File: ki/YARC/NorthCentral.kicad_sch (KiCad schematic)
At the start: 0 parts

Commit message: Continue annotating and labeling ICs
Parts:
- added U102, U103: 74HC245, symbol 74xx:74HC245
- added U88: 74HC00, symbol 74xx:74HC00
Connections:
- new net: U102.19 (CE), U103.19 (CE), U88.11
- new net GND: U102.10 (GND), U103.10 (GND)
- new net S1BUS0: U103.2 (A0)
- new net S1BUS15: U102.9 (A7)
- new net S1BUS7: U103.9 (A7)
- new net S1BUS8: U102.2 (A0)
- new net SYSADDR0: U103.18 (B0)
- new net SYSADDR15: U102.11 (B7)
- new net SYSADDR7: U103.11 (B7)
- new net SYSADDR8: U102.18 (B0)
- new net VCC: U102.1 (A->B), U102.20 (VCC), U103.1 (A->B), U103.20 (VCC)
- new net YARC/~{NANO}: U88.12, U88.13
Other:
- note added: "THIS SHEET IS ACTUALLY "EAST" CENTRAL"

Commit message: Minor changes while wiring Port1 address transceiver
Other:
- note added: "<== THIS IS WRONG - the signal comes from a '157. TODO."
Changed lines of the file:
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@@
+    (effects (font (size 1.27 1.27)) (justify left bottom))
+  )
+  (text "<== THIS IS WRONG - the signal comes from a '157. TODO."
+    (at 38.1 124.46 0)
     (effects (font (size 1.27 1.27)) (justify left bottom))
   )

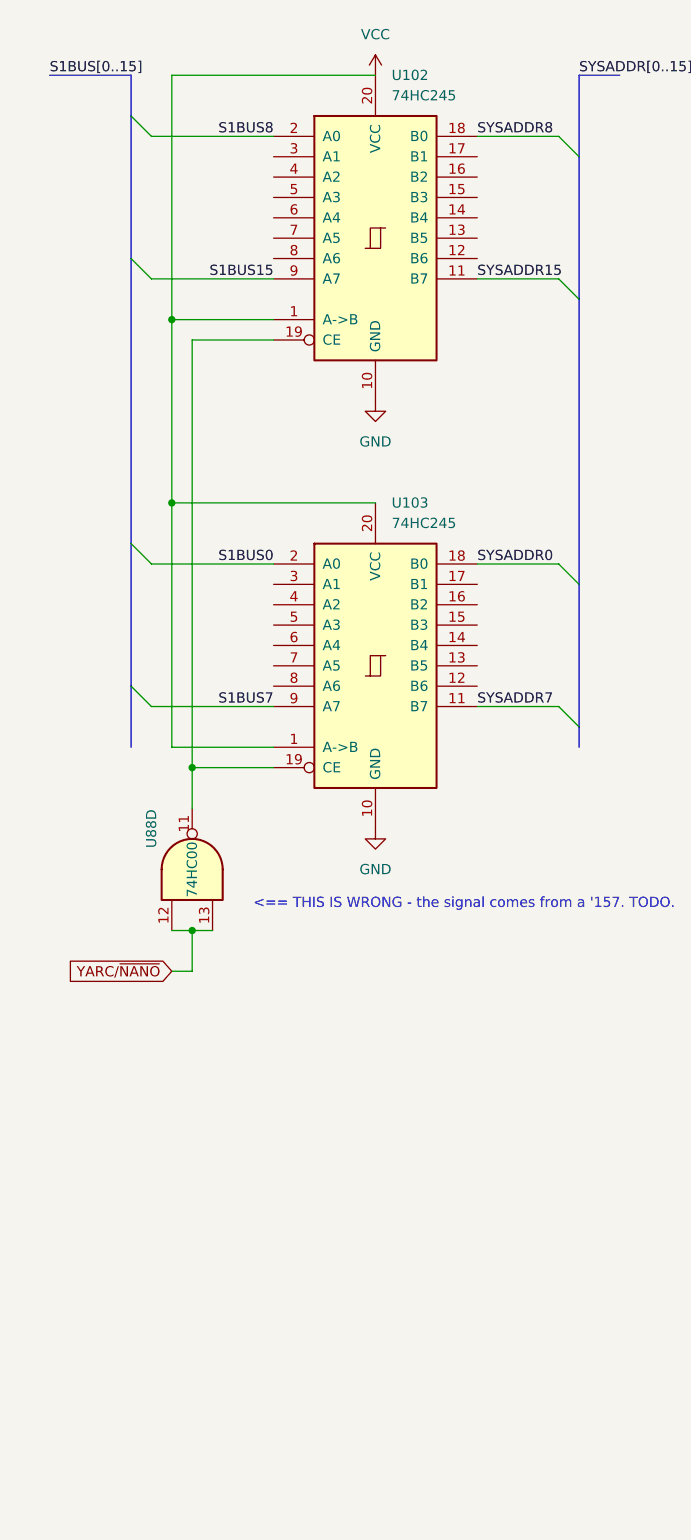
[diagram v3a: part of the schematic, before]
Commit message: Further development of ALU controls
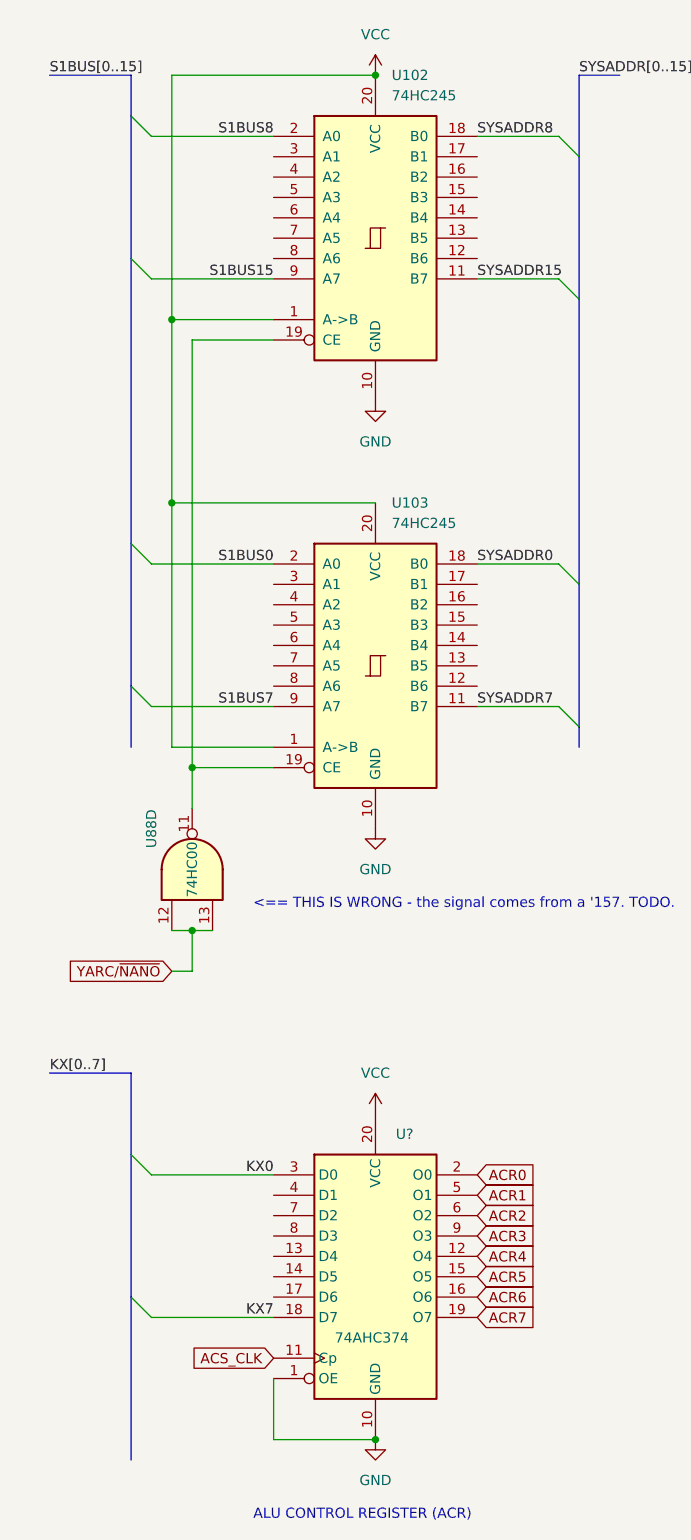
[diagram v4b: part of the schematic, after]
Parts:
- added U?: 74AHC374, symbol 74xx:74AHC374
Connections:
- net GND: now also U?.1 (OE), U?.10 (GND)
- net VCC: now also U?.20 (VCC)
- new net ACR0: U?.2 (O0)
- new net ACR1: U?.5 (O1)
- new net ACR2: U?.6 (O2)
- new net ACR3: U?.9 (O3)
- new net ACR4: U?.12 (O4)
- new net ACR5: U?.15 (O5)
- new net ACR6: U?.16 (O6)
- new net ACR7: U?.19 (O7)
- new net ACS_CLK: U?.11 (Cp)
- new net KX0: U?.3 (D0)
- new net KX7: U?.18 (D7)
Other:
- note added: "ALU CONTROL REGISTER (ACR)"

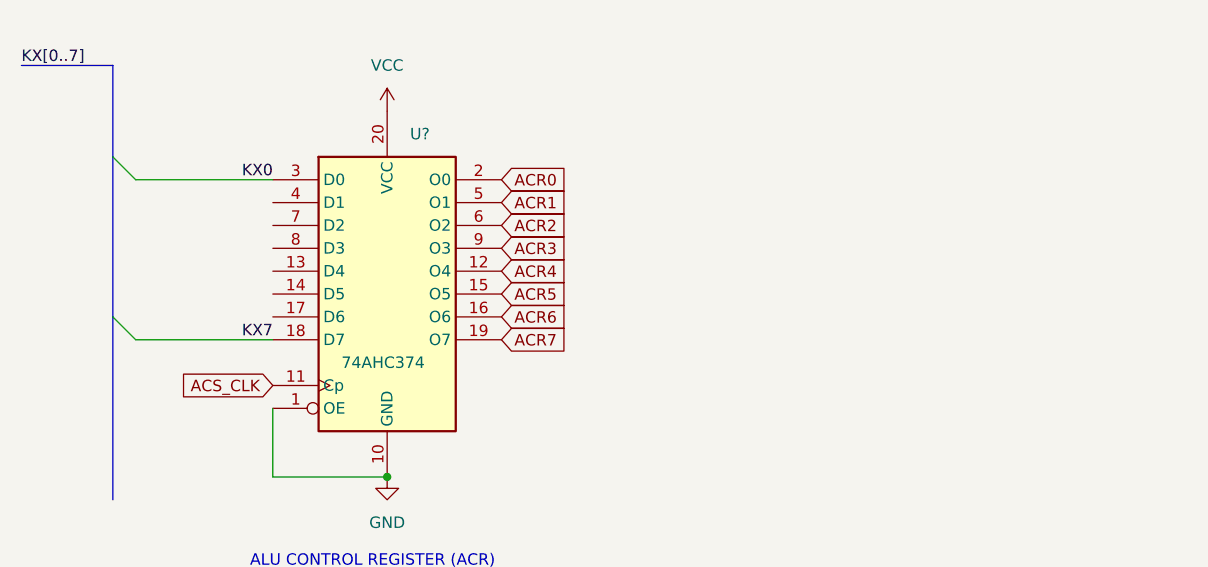
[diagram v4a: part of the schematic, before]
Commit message: ALU schematic checking complete. Ready to start layout.
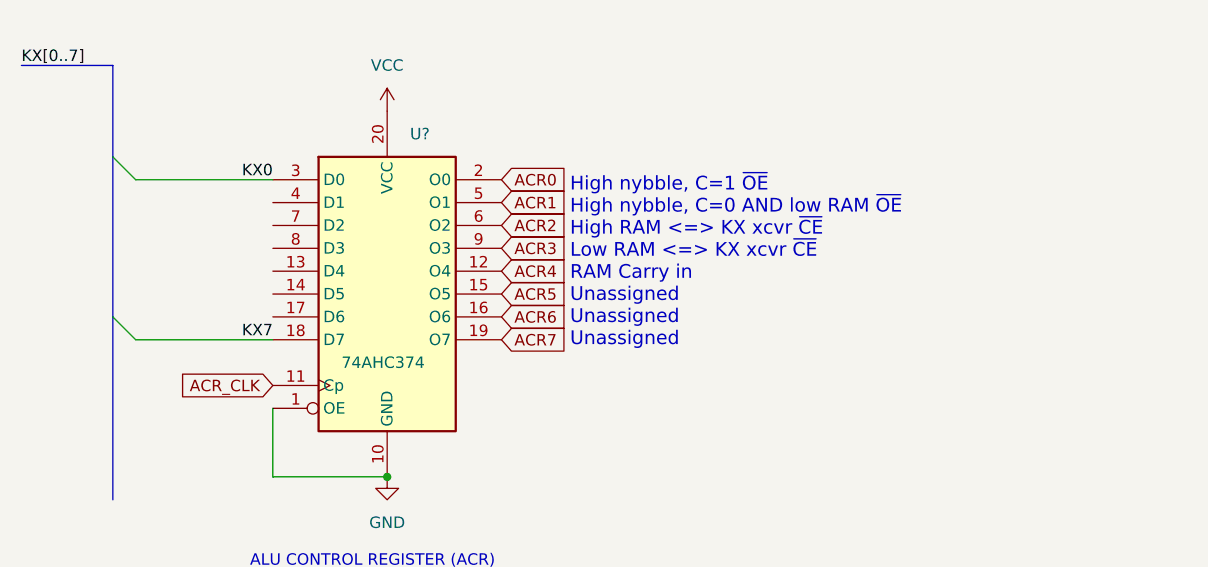
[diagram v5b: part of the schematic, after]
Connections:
- net ACS_CLK renamed ACR_CLK
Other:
- note added: "High nybble, C=1 ~{OE} High nybble, C=0 AND low RAM ~{OE} High RAM <=> KX xcvr ~{CE} Low RAM <=> KX xcvr ~{CE} RAM Carry in Unassigned Unassigned Unassigned"
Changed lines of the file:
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@@
     (stroke (width 0) (type default) (color 0 0 0 0))
+  )
+  (text "High nybble, C=1 ~{OE}\nHigh nybble, C=0 AND low RAM ~{OE}\nHigh RAM <=> KX xcvr ~{CE}\nLow RAM <=> KX xcvr ~{CE}\nRAM Carry in\nUnassigned\nUnassigned\nUnassigned"
+    (at 73.66 176.1744 0)
+    (effects (font (size 1.524 1.524)) (justify left bottom))
   )
   (text "THIS SHEET IS ACTUALLY \"EAST\" CENTRAL" (at 177.8 15.24 0)
@@
     )
   )
-  (global_label "ACS_CLK" (shape input) (at 40.64 180.34 180) (fields_autoplaced)
+  (global_label "ACR_CLK" (shape input) (at 40.64 180.34 180) (fields_autoplaced)
     (effects (font (size 1.27 1.27)) (justify right))
-    (property "Intersheet References" "${INTERSHEET_REFS}" (id 0) (at 30.1231 180.2606 0)
+    (property "Intersheet References" "${INTERSHEET_REFS}" (id 0) (at 30.0626 180.2606 0)
       (effects (font (size 1.27 1.27)) (justify right) hide)
     )

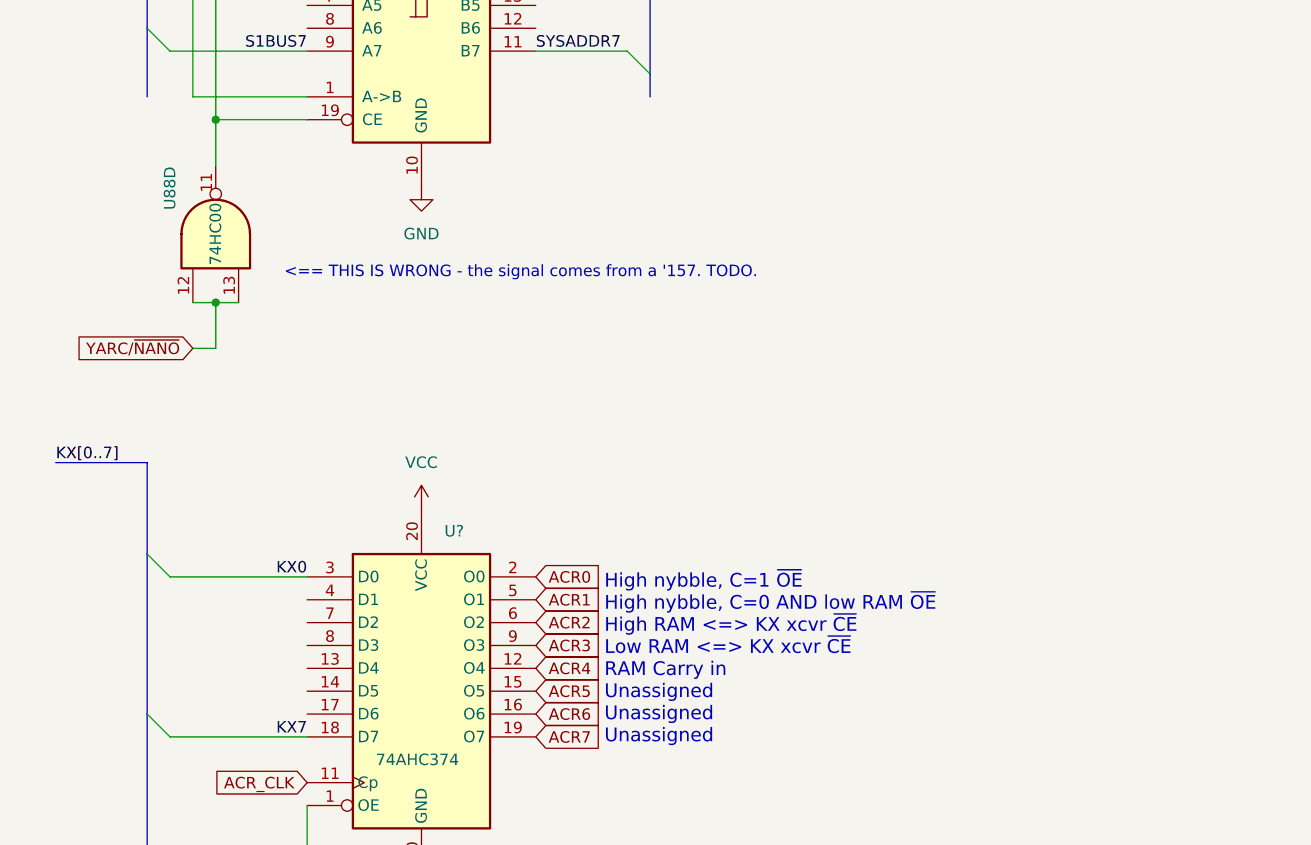
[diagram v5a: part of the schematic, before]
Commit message: Improvements to ALU and Flags schematic. Begin work on layout.
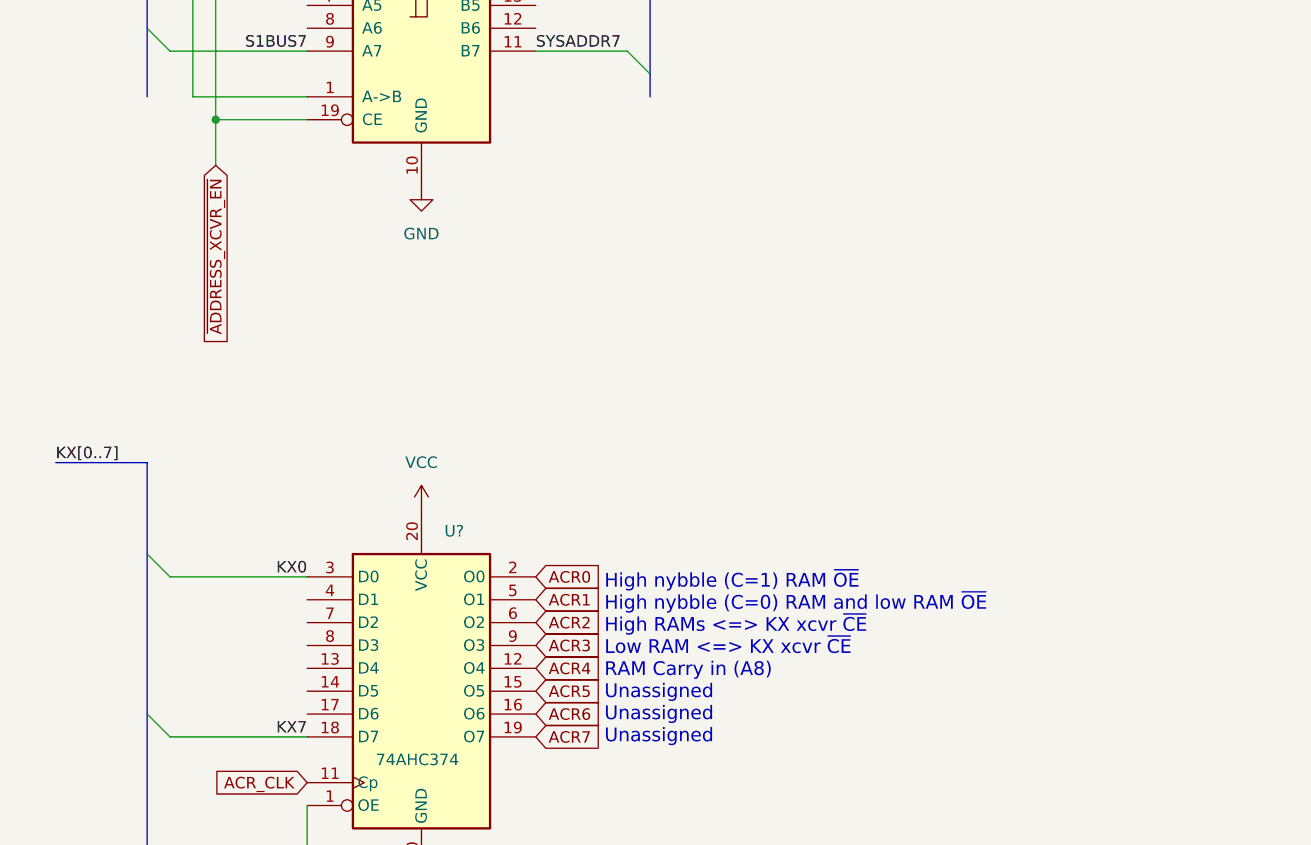
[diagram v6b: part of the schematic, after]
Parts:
- removed U88: 74HC00, symbol 74xx:74HC00
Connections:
- net ~{ADDRESS_XCVR_EN}: now reaches U102.19 (CE), U103.19 (CE)
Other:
- note added: "High nybble (C=1) RAM ~{OE} High nybble (C=0) RAM and low RAM ~{OE} High RAMs <=> KX xcvr ~{CE} Low RAM <=> KX xcvr ~{CE} RAM Carry in (A8) Unassigned Unassigned Unassigned"
- note removed: "<== THIS IS WRONG - the signal comes from a '157. TODO."
- note removed: "High nybble, C=1 ~{OE} High nybble, C=0 AND low RAM ~{OE} High RAM <=> KX xcvr ~{CE} Low RAM <=> KX xcvr ~{CE} RAM Carry in Unassigned Unassigned Unassigned"
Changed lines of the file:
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@@
     (comment 1 "All ICs are HC family regardless of P/N shown")
   )
-  (junction (at 30.48 127) (diameter 0) (color 0 0 0 0)
-  )
   (junction (at 53.34 190.5) (diameter 0) (color 0 0 0 0)
   )
@@
     (stroke (width 0) (type default) (color 0 0 0 0))
   )
-  (wire (pts (xy 27.94 132.08) (xy 30.48 132.08))
-    (stroke (width 0) (type default) (color 0 0 0 0))
-  )
   (wire (pts (xy 25.4 157.48) (xy 40.64 157.48))
     (stroke (width 0) (type default) (color 0 0 0 0))
@@
     (stroke (width 0) (type default) (color 0 0 0 0))
   )
-  (wire (pts (xy 30.48 127) (xy 33.02 127))
-    (stroke (width 0) (type default) (color 0 0 0 0))
-  )
   (bus (pts (xy 22.86 144.78) (xy 22.86 154.94))
     (stroke (width 0) (type default) (color 0 0 0 0))
@@
     (stroke (width 0) (type default) (color 0 0 0 0))
   )
-  (wire (pts (xy 27.94 127) (xy 30.48 127))
-    (stroke (width 0) (type default) (color 0 0 0 0))
-  )
   (bus (pts (xy 22.86 172.72) (xy 22.86 193.04))
     (stroke (width 0) (type default) (color 0 0 0 0))
@@
     (stroke (width 0) (type default) (color 0 0 0 0))
   )
-  (wire (pts (xy 30.48 132.08) (xy 30.48 127))
-    (stroke (width 0) (type default) (color 0 0 0 0))
-  )
   (bus (pts (xy 12.7 20.32) (xy 22.86 20.32))
     (stroke (width 0) (type default) (color 0 0 0 0))
@@
     (stroke (width 0) (type default) (color 0 0 0 0))
   )
-  (text "High nybble, C=1 ~{OE}\nHigh nybble, C=0 AND low RAM ~{OE}\nHigh RAM <=> KX xcvr ~{CE}\nLow RAM <=> KX xcvr ~{CE}\nRAM Carry in\nUnassigned\nUnassigned\nUnassigned"
+  (text "High nybble (C=1) RAM ~{OE}\nHigh nybble (C=0) RAM and low RAM ~{OE}\nHigh RAMs <=> KX xcvr ~{CE}\nLow RAM <=> KX xcvr ~{CE}\nRAM Carry in (A8)\nUnassigned\nUnassigned\nUnassigned"
     (at 73.66 176.1744 0)
     (effects (font (size 1.524 1.524)) (justify left bottom))
@@
   )
   (text "ALU CONTROL REGISTER (ACR)" (at 38.1 200.66 0)
-    (effects (font (size 1.27 1.27)) (justify left bottom))
-  )
-  (text "<== THIS IS WRONG - the signal comes from a '157. TODO."
-    (at 38.1 124.46 0)
     (effects (font (size 1.27 1.27)) (justify left bottom))
   )
@@
     )
   )
-  (global_label "YARC{slash}~{NANO}" (shape input) (at 27.94 132.08 180) (fields_autoplaced)
+  (global_label "~{ADDRESS_XCVR_EN}" (shape input) (at 30.48 111.76 270) (fields_autoplaced)
     (effects (font (size 1.27 1.27)) (justify right))
-    (property "Intersheet References" "${INTERSHEET_REFS}" (id 0) (at 14.3993 132.0006 0)
+    (property "Intersheet References" "${INTERSHEET_REFS}" (id 0) (at 30.5594 131.8926 90)
       (effects (font (size 1.27 1.27)) (justify right) hide)
     )
@@
     (pin "1")
   )
-  (symbol (lib_id "74xx:74HC00") (at 30.48 119.38 90) (unit 4)
-    (in_bom yes) (on_board yes)
-    (property "Reference" "U88" (id 0) (at 25.4 114.3 0))
-    (property "Value" "74HC00" (id 1) (at 30.48 119.38 0))
-    (property "Footprint" "" (id 2) (at 30.48 119.38 0)
-      (effects (font (size 1.27 1.27)) hide)
-    )
-    (property "Datasheet" "http://www.ti.com/lit/gpn/sn74hc00" (id 3) (at 30.48 119.38 0)
-      (effects (font (size 1.27 1.27)) hide)
-    )
-    (pin "11")
-    (pin "12")
-    (pin "13")
-  )
   (symbol (lib_id "74xx:74HC245") (at 53.34 93.98 0) (unit 1)
